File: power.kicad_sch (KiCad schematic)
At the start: 35 parts, among them IC301 XL1509-5.0E1, IC302 SY8113BADC, X301 KF2EDGR-3.81-3P, X302 USB3.1C16PFSMT, X303 CH340G, Y301 X322512MSB4SI

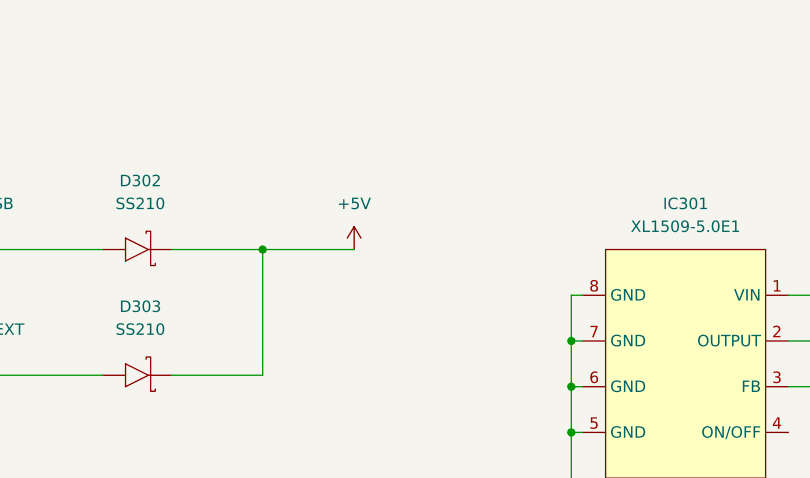
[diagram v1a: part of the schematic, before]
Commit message: Rough pcb placement for space estimation. Exchanged 40P connector
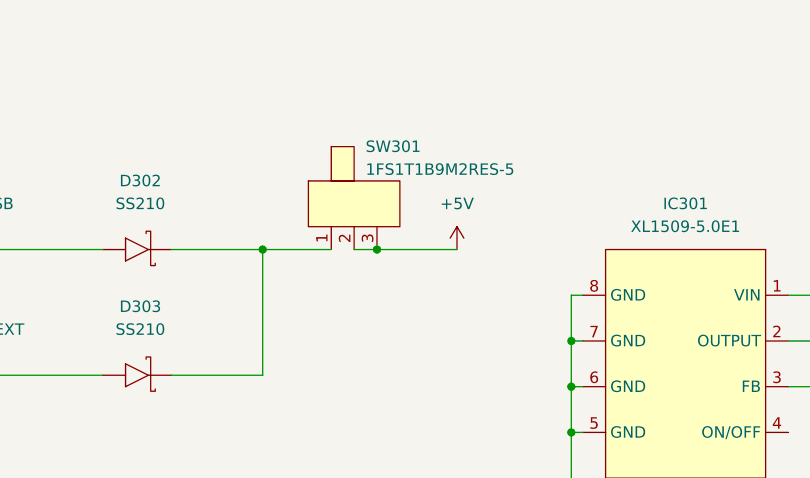
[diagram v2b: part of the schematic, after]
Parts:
- added SW301: 1FS1T1B9M2RES-5, SW-TH_1FS1T1B9M2RES-5, symbol eduboardv2:1FS1T1B9M2RES-5
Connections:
- net +5V: now also SW301.2, SW301.3; no longer D302.1 (K), D303.1 (K)
- new net: D302.1 (K), D303.1 (K), SW301.1
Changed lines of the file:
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@@
   (junction (at 64.77 62.23) (diameter 0) (color 0 0 0 0)
   )
+  (junction (at 134.62 39.37) (diameter 0) (color 0 0 0 0)
+  )
   (junction (at 110.49 166.37) (diameter 0) (color 0 0 0 0)
   )
@@
     (stroke (width 0) (type default) (color 0 0 0 0))
   )
-  (wire (pts (xy 121.92 39.37) (xy 132.08 39.37))
+  (wire (pts (xy 121.92 39.37) (xy 129.54 39.37))
     (stroke (width 0) (type default) (color 0 0 0 0))
   )
@@
     (stroke (width 0) (type default) (color 0 0 0 0))
   )
+  (wire (pts (xy 132.08 39.37) (xy 134.62 39.37))
+    (stroke (width 0) (type default) (color 0 0 0 0))
+  )
   (wire (pts (xy 63.5 134.62) (xy 68.58 134.62))
     (stroke (width 0) (type default) (color 0 0 0 0))
@@
   )
   (wire (pts (xy 215.9 49.53) (xy 227.33 49.53))
+    (stroke (width 0) (type default) (color 0 0 0 0))
+  )
+  (wire (pts (xy 134.62 39.37) (xy 143.51 39.37))
     (stroke (width 0) (type default) (color 0 0 0 0))
   )
@@
     (pin "1")
   )
-  (symbol (lib_id "eduboardv2:+5V") (at 132.08 39.37 0) (unit 1)
-    (in_bom yes) (on_board yes) (fields_autoplaced)
-    (property "Reference" "#PWR0319" (id 0) (at 132.08 43.18 0)
-      (effects (font (size 1.27 1.27)) hide)
-    )
-    (property "Value" "+5V" (id 1) (at 132.08 34.29 0))
-    (property "Footprint" "" (id 2) (at 132.08 39.37 0)
-      (effects (font (size 1.27 1.27)) hide)
-    )
-    (property "Datasheet" "" (id 3) (at 132.08 39.37 0)
+  (symbol (lib_id "eduboardv2:+5V") (at 143.51 39.37 0) (unit 1)
+    (in_bom yes) (on_board yes) (fields_autoplaced)
+    (property "Reference" "#PWR0319" (id 0) (at 143.51 43.18 0)
+      (effects (font (size 1.27 1.27)) hide)
+    )
+    (property "Value" "+5V" (id 1) (at 143.51 34.29 0))
+    (property "Footprint" "" (id 2) (at 143.51 39.37 0)
+      (effects (font (size 1.27 1.27)) hide)
+    )
+    (property "Datasheet" "" (id 3) (at 143.51 39.37 0)
       (effects (font (size 1.27 1.27)) hide)
     )
@@
     (pin "2")
   )
+  (symbol (lib_id "eduboardv2:1FS1T1B9M2RES-5") (at 132.08 34.29 0) (unit 1)
+    (in_bom yes) (on_board yes)
+    (property "Reference" "SW301" (id 0) (at 133.35 27.94 0)
+      (effects (font (size 1.27 1.27)) (justify left))
+    )
+    (property "Value" "1FS1T1B9M2RES-5" (id 1) (at 133.35 30.48 0)
+      (effects (font (size 1.27 1.27)) (justify left))
+    )
+    (property "Footprint" "SW-TH_1FS1T1B9M2RES-5" (id 2) (at 132.08 46.99 0)
+      (effects (font (size 1.27 1.27)) hide)
+    )
+    (property "Datasheet" "https://lcsc.com/product-detail/New-Arrivals_Dailywell-1FS1T1B9M2RES-5_C496164.html" (id 3) (at 132.08 52.07 0)
+      (effects (font (size 1.27 1.27)) hide)
+    )
+    (property "Manufacturer" "Dailywell" (id 4) (at 132.08 54.61 0)
+      (effects (font (size 1.27 1.27)) hide)
+    )
+    (property "LCSC Part" "C496164" (id 5) (at 132.08 57.15 0)
+      (effects (font (size 1.27 1.27)) hide)
+    )
+    (property "JLC Part" "Extended Part" (id 6) (at 132.08 59.69 0)
+      (effects (font (size 1.27 1.27)) hide)
+    )
+    (property "MPN" "1FS1T1B9M2RES-5" (id 7) (at 132.08 44.45 0)
+      (effects (font (size 1.27 1.27)) hide)
+    )
+    (pin "1")
+    (pin "2")
+    (pin "3")
+  )
   (symbol (lib_id "eduboardv2:GND") (at 102.87 160.02 0) (unit 1)

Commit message: changed pin types and fixed 3D-positions
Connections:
- net +3.3V: no longer names the net of C308.2, C310.2, C312.1, C314.1, C316.1, D305.1 (A), L301.2, R305.2
- net +5V: no longer names the net of C307.2, IC302.5 (IN), R303.2
- net +5V: no longer SW301.2, SW301.3
- net +5V_EXT: no longer names the net of C309.1, C311.1, C313.2, C315.1, IC301.3 (FB), L302.2
- net +5V_EXT: no longer D303.2 (A)
- removed net GND: C301.2, C302.1, C303.1, C304.1, C305.1, C307.1, C309.2, C310.1, C311.2, C312.2, C313.1, C314.2, C315.2, C316.2, D301.2 (A), D304.2 (A), IC301.5 (GND), IC301.6 (GND), IC301.7 (GND), IC301.8 (GND), IC302.2 (GND), R301.2, R302.1, R304.1, R306.1, X301.3, X302.0, X302.A1 (GND), X302.A12 (GND), X303.1 (GND), Y301.2 (GND), Y301.4 (GND)
- net V_EXT: no longer names the net of C301.1, D301.1 (K), X301.1
- net V_EXT: no longer IC301.1 (VIN)
- removed net V_USB: C305.2, D302.2 (A), X302.A4 (VBUS), X302.A9 (VBUS), X303.16 (VCC)
- new net: X302.A4 (VBUS), X302.A9 (VBUS)
- new net: D301.2 (A), X301.3
- new net: C305.2, X303.16 (VCC)
- new net: IC301.5 (GND), IC301.6 (GND), IC301.7 (GND), IC301.8 (GND)
- new net: SW301.2, SW301.3

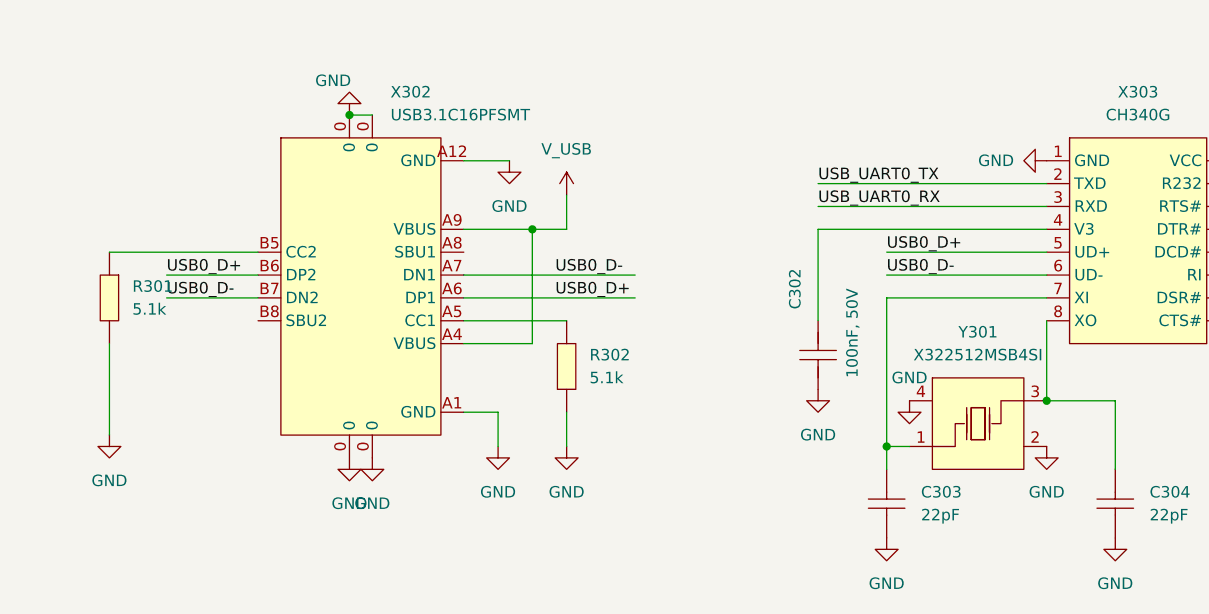
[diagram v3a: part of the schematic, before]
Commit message: change all local labels to global labels.
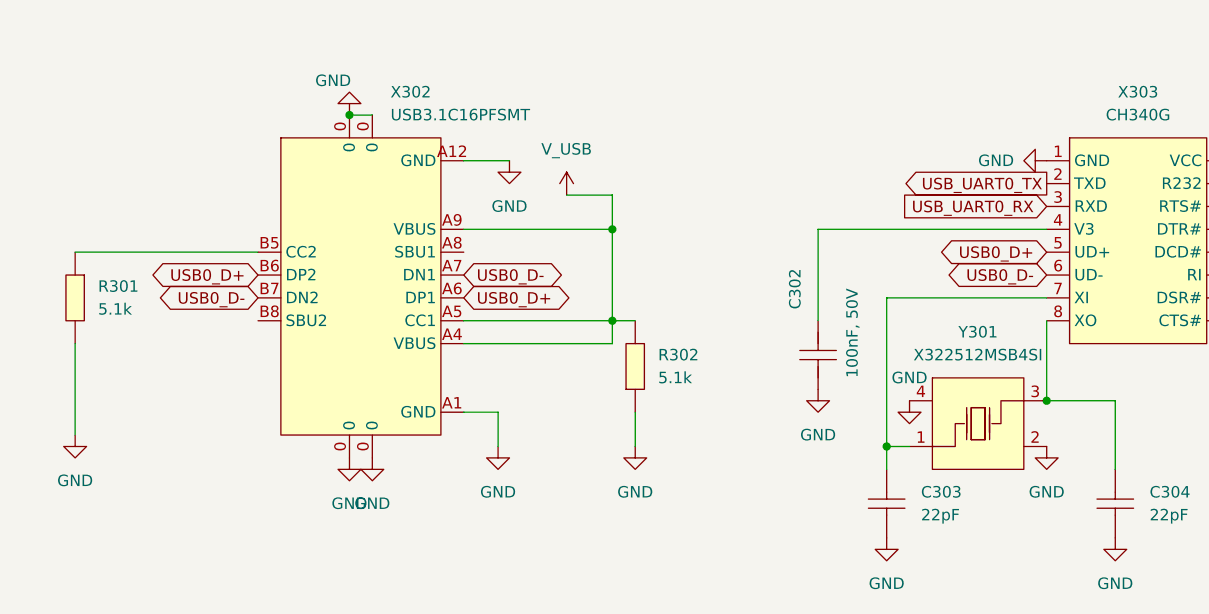
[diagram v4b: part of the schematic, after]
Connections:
- net at X302.A4 (VBUS), X302.A9 (VBUS): now also R302.2, X302.A5 (CC1)
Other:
- moved on the sheet: R301, R302

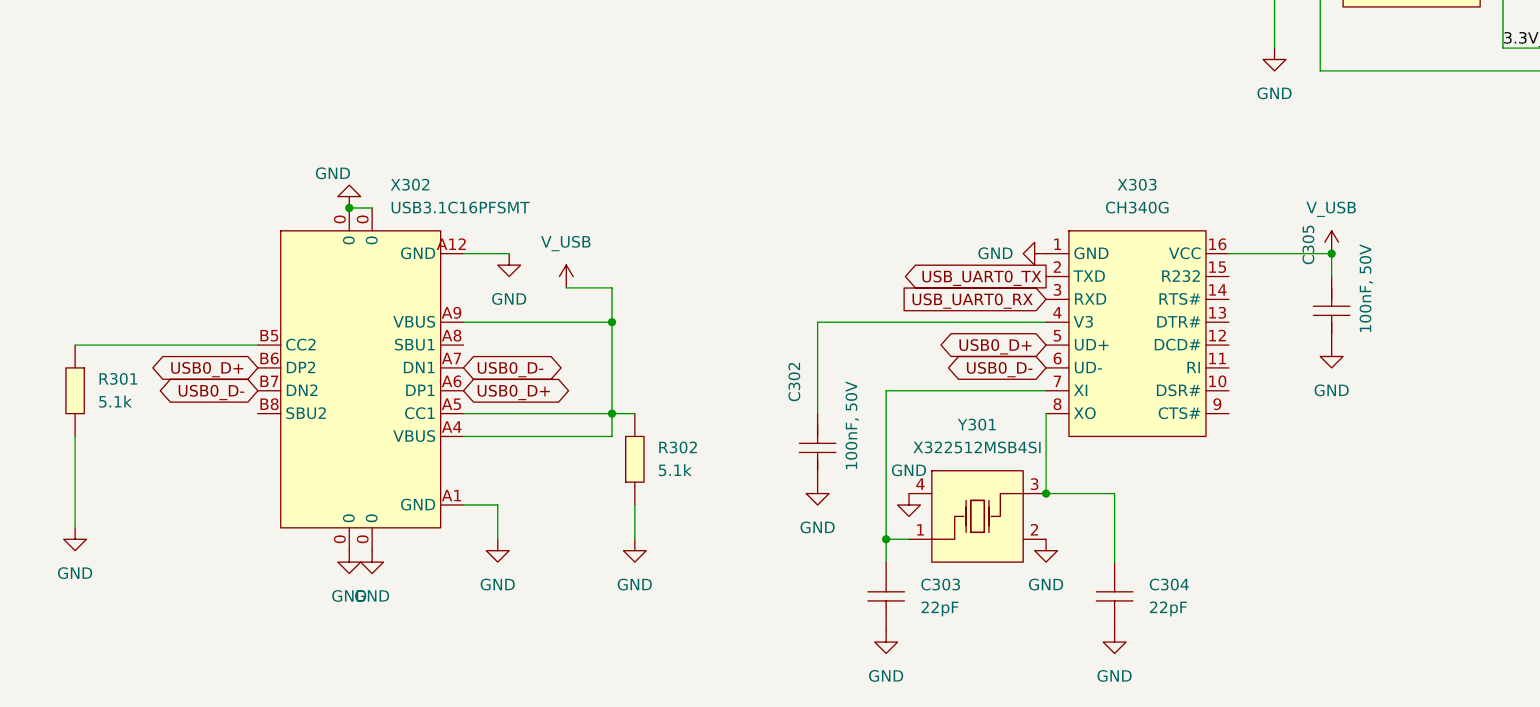
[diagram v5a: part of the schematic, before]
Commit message: move USB Serial Converter and USB Connector to correct pages
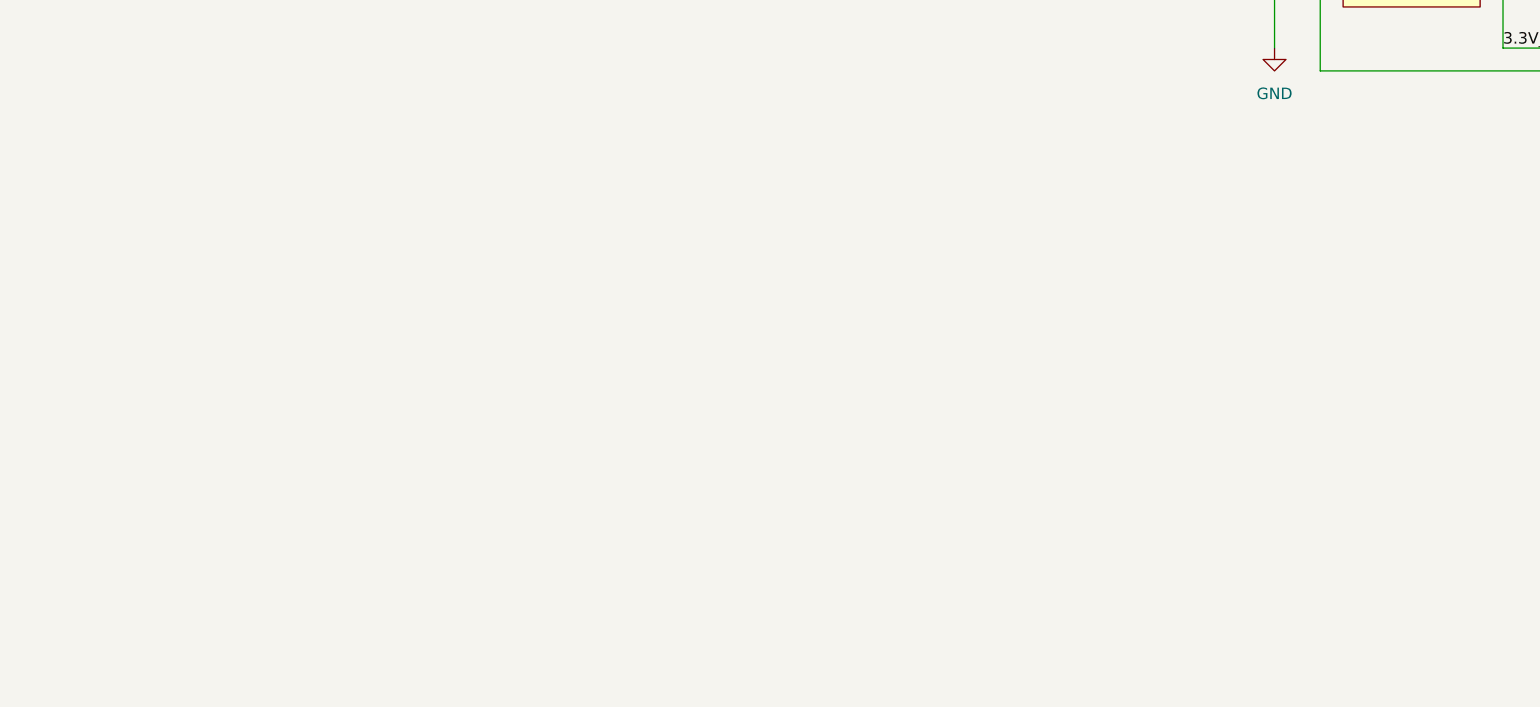
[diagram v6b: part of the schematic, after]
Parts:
- removed C302, C305: 100nF, 50V, C0402, symbol eduboardv2:CL05B104KB54PNC
- removed C303, C304: 22pF, C0402, symbol eduboardv2:0402CG220J500NT
- removed R301, R302: 5.1k, R0402, symbol eduboardv2:0402WGF5101TCE
- removed X302: USB3.1C16PFSMT, USB-C-SMD_TYPE-C-USB-17, symbol eduboardv2:USB3.1C16PFSMT
- removed X303: CH340G, SOIC-16_L9.9-W3.9-P1.27-LS6.0-BL, symbol eduboardv2:CH340G
- removed Y301: X322512MSB4SI, OSC-SMD_4P-L3.2-W2.5-BL, symbol eduboardv2:X322512MSB4SI

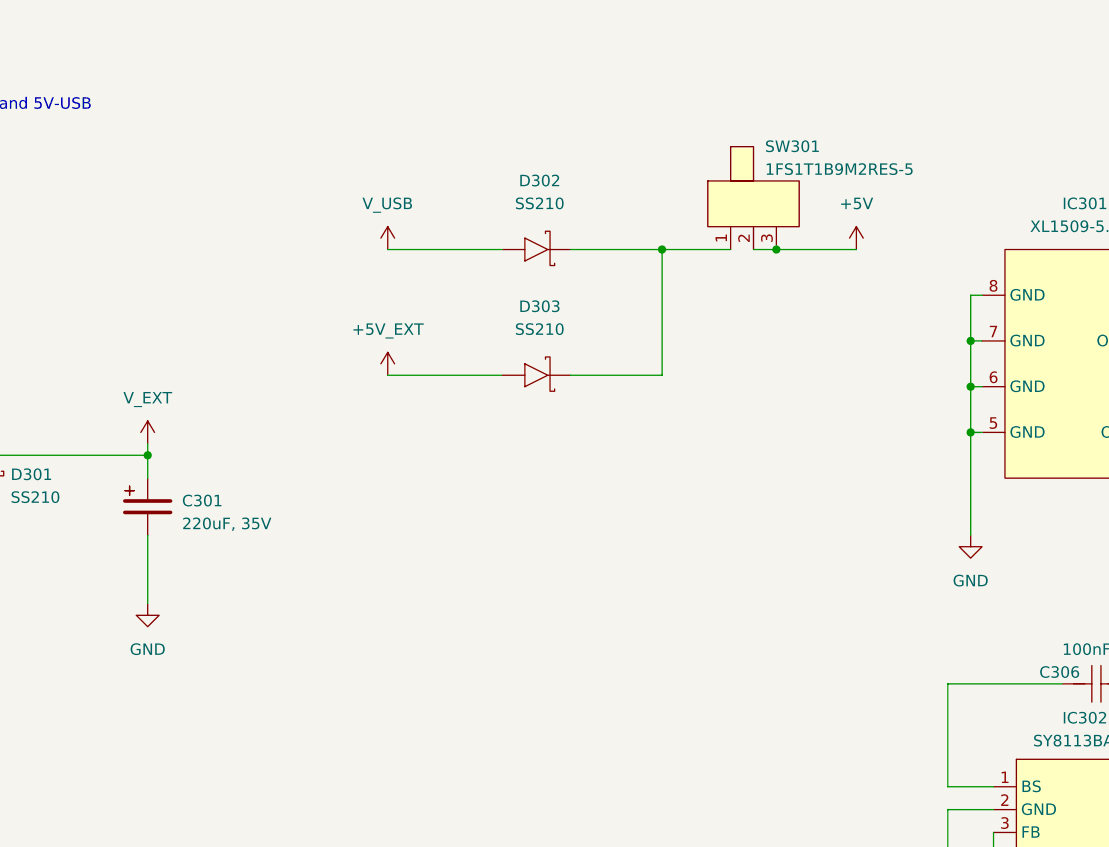
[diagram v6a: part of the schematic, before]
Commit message: change voltage selector
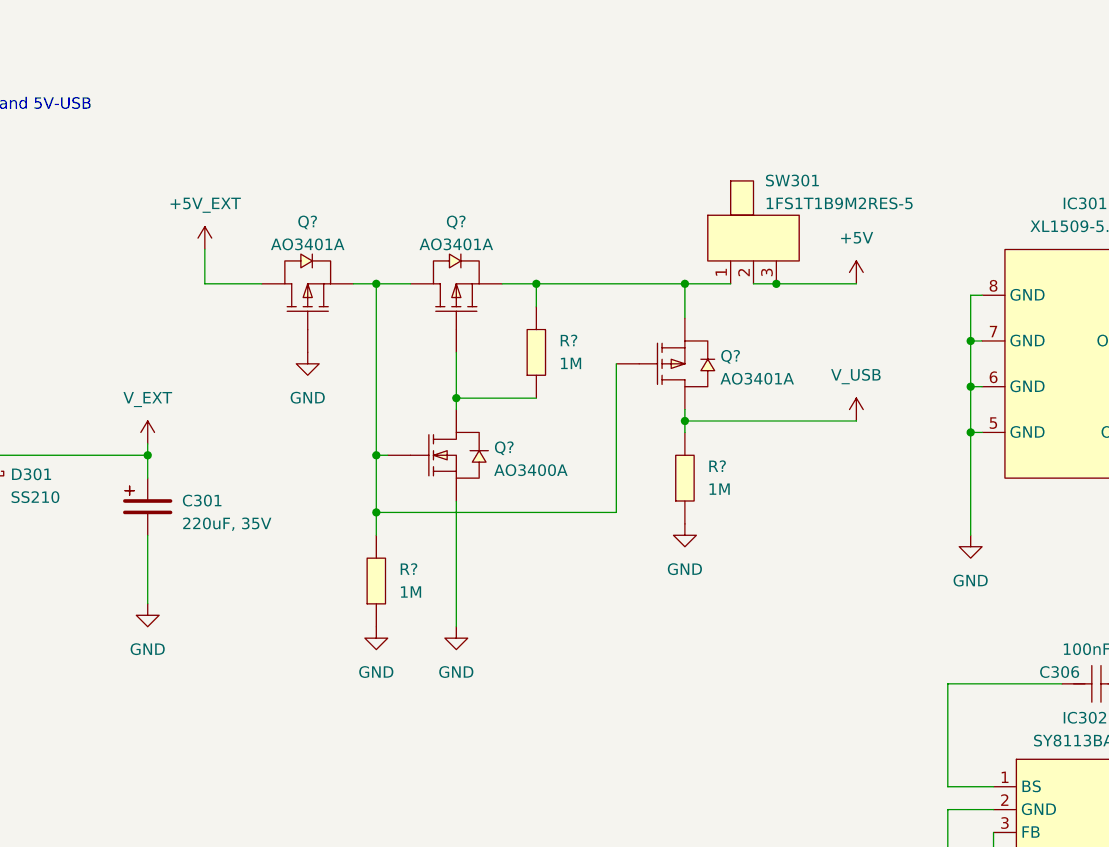
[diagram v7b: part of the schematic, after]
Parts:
- removed D302, D303: SS210, SMA_L4.3-W2.6-LS5.2-RD, symbol eduboardv2:SS210
- added Q? (x3): AO3401A, SOT-23_L2.9-W1.3-P1.90-LS2.4-BR, symbol eduboardv2:AO3401A
- added Q?: AO3400A, SOT-23-3_L2.9-W1.6-P1.90-LS2.8-BR, symbol eduboardv2:AO3400A
- added R? (x3): 1M, R0402, symbol eduboardv2:0402WGF1003TCE
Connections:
- net at SW301.1: now also Q?.2 (S), Q?.2 (S), R?.2
- new net: Q?.1 (G), Q?.3 (D), R?.1
- new net: Q?.1 (G), Q?.1 (G), Q?.2 (S), Q?.3 (D), R?.2
- new net: Q?.3 (D), R?.2
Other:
- moved on the sheet: SW301
